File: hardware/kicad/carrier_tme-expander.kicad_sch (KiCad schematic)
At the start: 9 parts, among them U2 TCA9534PWR

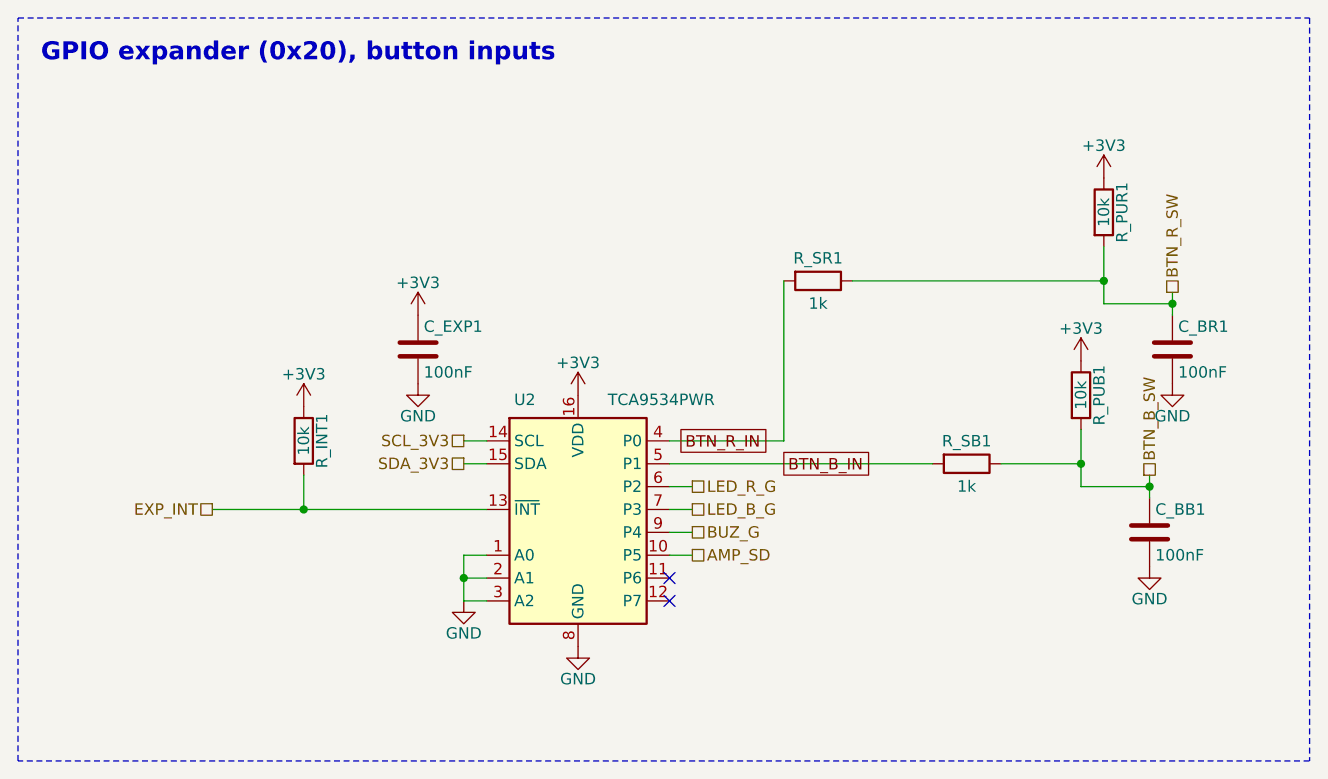
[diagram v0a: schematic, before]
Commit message: hardware: 3.5" ILI9488 SPI TFT replaces the Newhaven LCD
Carrier and carrier_tme: J_LCD1 XH-8 (VCC GND CS RST DC MOSI SCK LED,
the module header order; CS tied low). SPI3 on GPIO43/44, PWM backlight
on GPIO6 (R_BLPD1), DC/RST on TCA9534 P6/P7, buttons polled. The P4/P5
native-pin option was dropped: the Heltec GNSS receptacle opens toward
those pins. Removed the I2C level shifter, R_INT1/EXP_INT and J_UART1;
J_NFC1 moved to the bottom edge. Both boards: 0 unrouted, ERC/DRC/parity 0.

Lid rebuilt from the LCDWiki MSP3520 drawing: 98 x 56.34, M3 bosses on
92 x 49.5 (r3.0, 4.5 high), 80 x 51 viewing window, 11.5 mm depth.
make mech green. Power model: backlight duty is now the mean PWM level.

Co-Authored-By: Claude Opus 5.5 <noreply@anthropic.com>
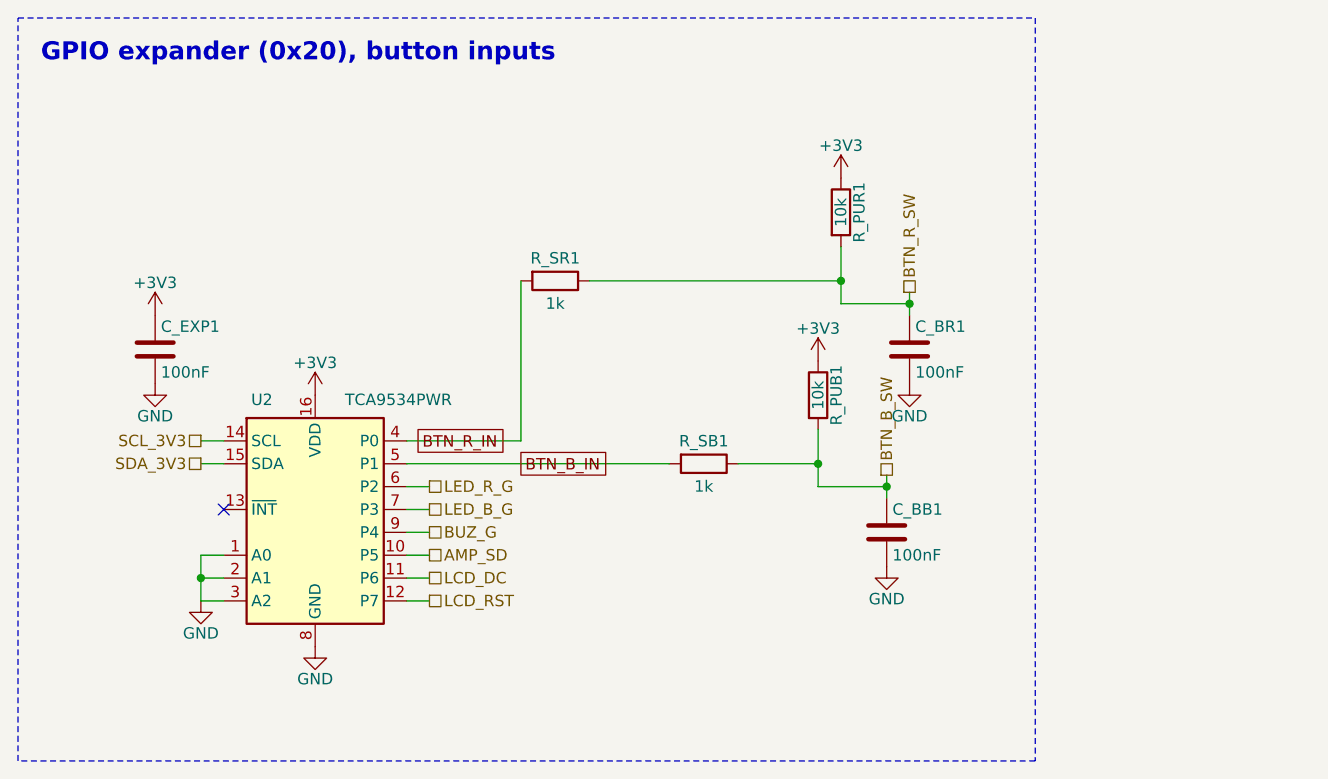
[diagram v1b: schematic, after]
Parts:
- removed R_INT1: 10k, Resistor_SMD:R_0805_2012Metric_Pad1.20x1.40mm_HandSolder, symbol Device:R
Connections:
- net LCD_DC: now reaches U2.11 (P6)
- net LCD_RST: now reaches U2.12 (P7)
- net EXP_INT: no longer names the net of U2.13 (~{INT})
- no-connect marks 2 -> 1
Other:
- moved on the sheet: C_BB1, C_BR1, C_EXP1, R_PUB1, R_PUR1, R_SB1, R_SR1, U2
